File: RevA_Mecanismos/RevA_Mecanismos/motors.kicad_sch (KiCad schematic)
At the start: 47 parts, among them J10 Screw_Terminal_01x02, J11 Screw_Terminal_01x02, J12 Conn_01x08_Socket, J13 Conn_01x08_Socket, J14 Conn_01x02_Pin, J15 430450624, J20 3557-2, J21 Conn_01x04_Pin, J22 Conn_01x04_Pin, J8 3557-2, J9 3557-2, Q3 IRF9540NSPBF, Q4 IRF9540NSPBF, Q5 IRF9540NSPBF, Q6 IRF9540NSPBF, U4 IRF540SPBF, U5 IRF540SPBF, U6 IRF540SPBF, U7 IRF540SPBF, U8 TXB0104D

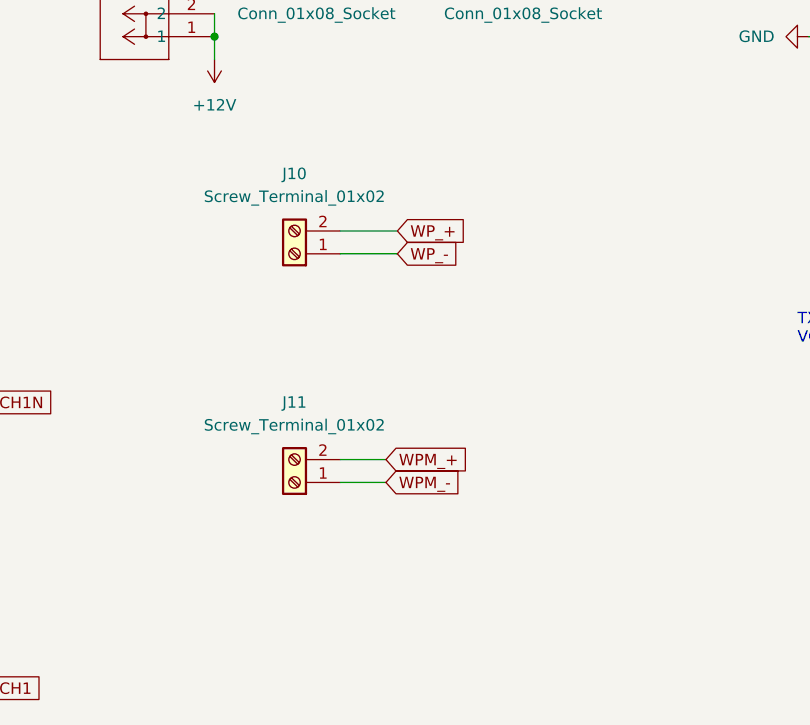
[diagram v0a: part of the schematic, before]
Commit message: Replacement of screw terminals for molex connectors
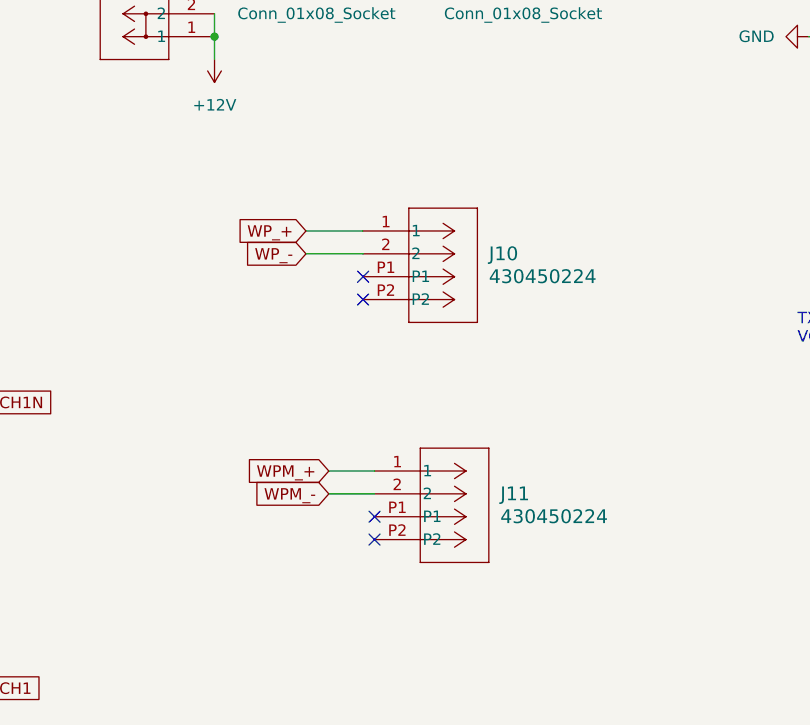
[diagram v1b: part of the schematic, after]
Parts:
- removed J10, J11: Screw_Terminal_01x02, symbol Connector:Screw_Terminal_01x02
- added J10, J11: 430450224, MolexConnectors:CON_430450224_MOL, symbol MolexConnectors:430450224
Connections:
- net WPM_+: now also J11.1
- net WPM_-: now also J11.2
- net WP_+: now also J10.1
- net WP_-: now also J10.2
- no-connect marks 8 -> 12
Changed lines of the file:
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@@
   (no_connect (at 238.76 50.8))
   (no_connect (at 238.76 55.88))
+  (no_connect (at 180.34 125.73))
+  (no_connect (at 180.34 128.27))
+  (no_connect (at 181.61 154.94))
   (no_connect (at 196.85 81.28))
   (no_connect (at 196.85 86.36))
@@
   (no_connect (at 196.85 88.9))
   (no_connect (at 196.85 78.74))
+  (no_connect (at 181.61 152.4))
   (wire (pts (xy 76.2 176.53) (xy 76.2 181.61))
     (stroke (width 0) (type default))
@@
     (stroke (width 0) (type default))
   )
-  (wire (pts (xy 177.8 123.19) (xy 184.15 123.19))
+  (wire (pts (xy 180.34 123.19) (xy 173.99 123.19))
     (stroke (width 0) (type default))
   )
@@
     (stroke (width 0) (type default))
   )
-  (wire (pts (xy 177.8 146.05) (xy 182.88 146.05))
+  (wire (pts (xy 181.61 147.32) (xy 176.53 147.32))
     (stroke (width 0) (type default))
   )
@@
     (stroke (width 0) (type default))
   )
-  (wire (pts (xy 177.8 120.65) (xy 184.15 120.65))
+  (wire (pts (xy 180.34 120.65) (xy 173.99 120.65))
     (stroke (width 0) (type default))
   )
@@
     (stroke (width 0) (type default))
   )
-  (wire (pts (xy 177.8 148.59) (xy 182.88 148.59))
-    (stroke (width 0) (type default))
-  )
   (wire (pts (xy 232.41 36.83) (xy 232.41 38.1))
     (stroke (width 0) (type default))
@@
   )
   (wire (pts (xy 113.03 139.7) (xy 110.49 139.7))
+    (stroke (width 0) (type default))
+  )
+  (wire (pts (xy 181.61 149.86) (xy 176.53 149.86))
     (stroke (width 0) (type default))
   )
@@
     )
   )
-  (global_label "WP_+" (shape input) (at 184.15 120.65 0)
-    (effects (font (size 1.27 1.27)) (justify left))
-    (property "Intersheetrefs" "${INTERSHEET_REFS}" (at 195.2233 120.7294 0)
-      (effects (font (size 1.27 1.27)) (justify left) hide)
+  (global_label "WP_+" (shape input) (at 173.99 120.65 180)
+    (effects (font (size 1.27 1.27)) (justify right))
+    (property "Intersheetrefs" "${INTERSHEET_REFS}" (at 162.9167 120.5706 0)
+      (effects (font (size 1.27 1.27)) (justify right) hide)
     )
   )
@@
     )
   )
-  (global_label "WP_-" (shape input) (at 184.15 123.19 0)
-    (effects (font (size 1.27 1.27)) (justify left))
-    (property "Intersheetrefs" "${INTERSHEET_REFS}" (at 195.2233 123.2694 0)
-      (effects (font (size 1.27 1.27)) (justify left) hide)
+  (global_label "WP_-" (shape input) (at 173.99 123.19 180)
+    (effects (font (size 1.27 1.27)) (justify right))
+    (property "Intersheetrefs" "${INTERSHEET_REFS}" (at 162.9167 123.1106 0)
+      (effects (font (size 1.27 1.27)) (justify right) hide)
     )
   )
@@
     )
   )
-  (global_label "WPM_+" (shape input) (at 182.88 146.05 0)
-    (effects (font (size 1.27 1.27)) (justify left))
-    (property "Intersheetrefs" "${INTERSHEET_REFS}" (at 193.9533 146.1294 0)
-      (effects (font (size 1.27 1.27)) (justify left) hide)
-    )
-  )
-  (global_label "WPM_-" (shape input) (at 182.88 148.59 0)
-    (effects (font (size 1.27 1.27)) (justify left))
-    (property "Intersheetrefs" "${INTERSHEET_REFS}" (at 193.9533 148.6694 0)
-      (effects (font (size 1.27 1.27)) (justify left) hide)
+  (global_label "WPM_+" (shape input) (at 176.53 147.32 180)
+    (effects (font (size 1.27 1.27)) (justify right))
+    (property "Intersheetrefs" "${INTERSHEET_REFS}" (at 165.4567 147.2406 0)
+      (effects (font (size 1.27 1.27)) (justify right) hide)
+    )
+  )
+  (global_label "WPM_-" (shape input) (at 176.53 149.86 180)
+    (effects (font (size 1.27 1.27)) (justify right))
+    (property "Intersheetrefs" "${INTERSHEET_REFS}" (at 165.4567 149.7806 0)
+      (effects (font (size 1.27 1.27)) (justify right) hide)
     )
   )
@@
     )
   )
-  (symbol (lib_id "Connector:Screw_Terminal_01x02") (at 172.72 123.19 180) (unit 1)
-    (in_bom yes) (on_board yes) (dnp no) (fields_autoplaced)
-    (property "Reference" "J10" (at 172.72 114.3 0)
-      (effects (font (size 1.27 1.27)))
-    )
-    (property "Value" "Screw_Terminal_01x02" (at 172.72 116.84 0)
-      (effects (font (size 1.27 1.27)))
-    )
-    (property "Footprint" "" (at 172.72 123.19 0)
-      (effects (font (size 1.27 1.27)) hide)
-    )
-    (property "Datasheet" "~" (at 172.72 123.19 0)
-      (effects (font (size 1.27 1.27)) hide)
-    )
-    (pin "1")
-    (pin "2")
-    (instances
-      (project "RevA_Mecanismos"
-        (path "/3a16a434-10b7-49a8-988b-273362cb395e/74867fa8-4aab-42a6-9e26-9663fc8ad5fc"
-          (reference "J10") (unit 1)
-        )
-      )
-    )
-  )
   (symbol (lib_id "power:GND") (at 209.55 43.18 270) (unit 1)
     (in_bom yes) (on_board yes) (dnp no) (fields_autoplaced)
@@
     )
   )
+  (symbol (lib_id "MolexConnectors:430450224") (at 180.34 120.65 0) (unit 1)
+    (in_bom yes) (on_board yes) (dnp no) (fields_autoplaced)
+    (property "Reference" "J10" (at 194.31 123.19 0)
+      (effects (font (size 1.524 1.524)) (justify left))
+    )
+    (property "Value" "430450224" (at 194.31 125.73 0)
+      (effects (font (size 1.524 1.524)) (justify left))
+    )
+    (property "Footprint" "MolexConnectors:CON_430450224_MOL" (at 180.34 120.65 0)
+      (effects (font (size 1.27 1.27) italic) hide)
+    )
+    (property "Datasheet" "430450224" (at 180.34 120.65 0)
+      (effects (font (size 1.27 1.27) italic) hide)
+    )
+    (pin "1")
+    (pin "2")
+    (pin "P1")
+    (pin "P2")
+    (instances
+      (project "RevA_Mecanismos"
+        (path "/3a16a434-10b7-49a8-988b-273362cb395e/74867fa8-4aab-42a6-9e26-9663fc8ad5fc"
+          (reference "J10") (unit 1)
+        )
+      )
+    )
+  )
   (symbol (lib_id "Device:R_Small") (at 49.53 80.01 270) (mirror x) (unit 1)
     (in_bom yes) (on_board yes) (dnp no)
@@
     )
   )
-  (symbol (lib_id "Connector:Screw_Terminal_01x02") (at 172.72 148.59 180) (unit 1)
-    (in_bom yes) (on_board yes) (dnp no) (fields_autoplaced)
-    (property "Reference" "J11" (at 172.72 139.7 0)
-      (effects (font (size 1.27 1.27)))
-    )
-    (property "Value" "Screw_Terminal_01x02" (at 172.72 142.24 0)
-      (effects (font (size 1.27 1.27)))
-    )
-    (property "Footprint" "" (at 172.72 148.59 0)
-      (effects (font (size 1.27 1.27)) hide)
-    )
-    (property "Datasheet" "~" (at 172.72 148.59 0)
-      (effects (font (size 1.27 1.27)) hide)
-    )
-    (pin "1")
-    (pin "2")
-    (instances
-      (project "RevA_Mecanismos"
-        (path "/3a16a434-10b7-49a8-988b-273362cb395e/74867fa8-4aab-42a6-9e26-9663fc8ad5fc"
-          (reference "J11") (unit 1)
-        )
-      )
-    )
-  )
   (symbol (lib_id "Device:C") (at 260.35 86.36 0) (unit 1)
     (in_bom yes) (on_board yes) (dnp no) (fields_autoplaced)
@@
         )
       )
+    )
+  )
+  (symbol (lib_id "MolexConnectors:430450224") (at 181.61 147.32 0) (unit 1)
+    (in_bom yes) (on_board yes) (dnp no) (fields_autoplaced)
+    (property "Reference" "J11" (at 195.58 149.86 0)
+      (effects (font (size 1.524 1.524)) (justify left))
+    )
+    (property "Value" "430450224" (at 195.58 152.4 0)
+      (effects (font (size 1.524 1.524)) (justify left))
+    )
+    (property "Footprint" "MolexConnectors:CON_430450224_MOL" (at 181.61 147.32 0)
+      (effects (font (size 1.27 1.27) italic) hide)
+    )
+    (property "Datasheet" "430450224" (at 181.61 147.32 0)
+      (effects (font (size 1.27 1.27) italic) hide)
+    )
+    (pin "1")
+    (pin "2")
+    (pin "P1")
+    (pin "P2")
+    (instances
+      (project "RevA_Mecanismos"
+        (path "/3a16a434-10b7-49a8-988b-273362cb395e/74867fa8-4aab-42a6-9e26-9663fc8ad5fc"
+          (reference "J11") (unit 1)
+        )
+      )
